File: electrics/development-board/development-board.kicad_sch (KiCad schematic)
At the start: 36 parts, among them J1 East, J10 Ext_5V, J8 West, J9 PinOut, Q3 S8050, Q4 S8050, SW1 Reset, SW2 Setup, SW3 Power, U1 LD1117S33

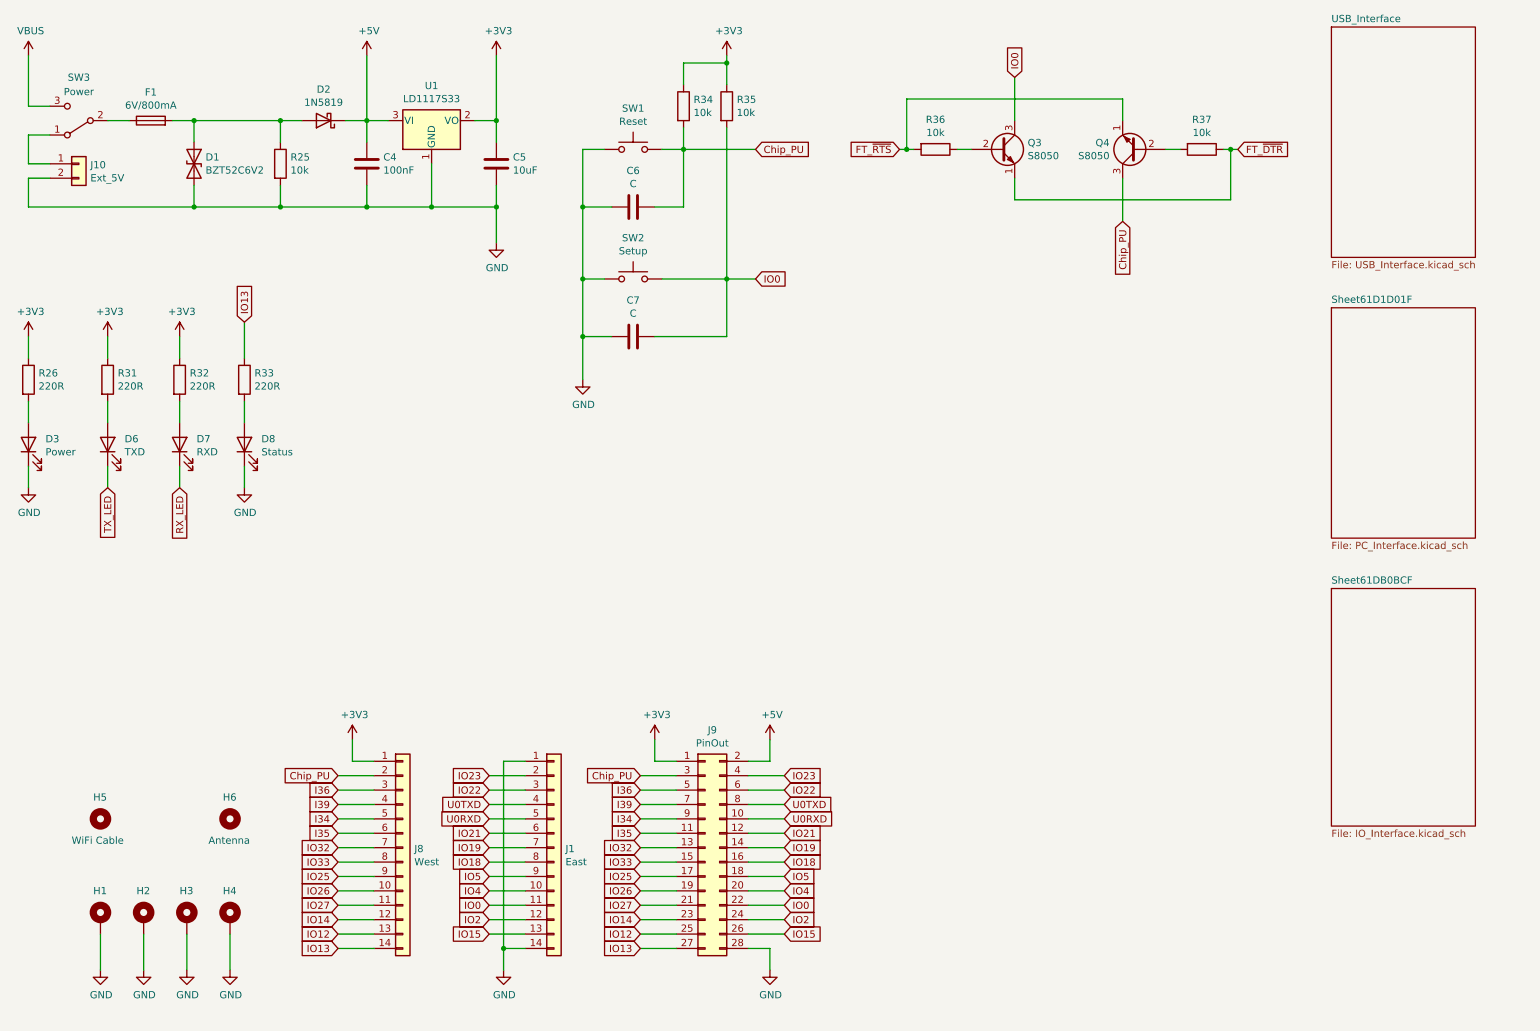
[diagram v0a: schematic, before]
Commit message: INOA-372 Rename Fab and Dev board
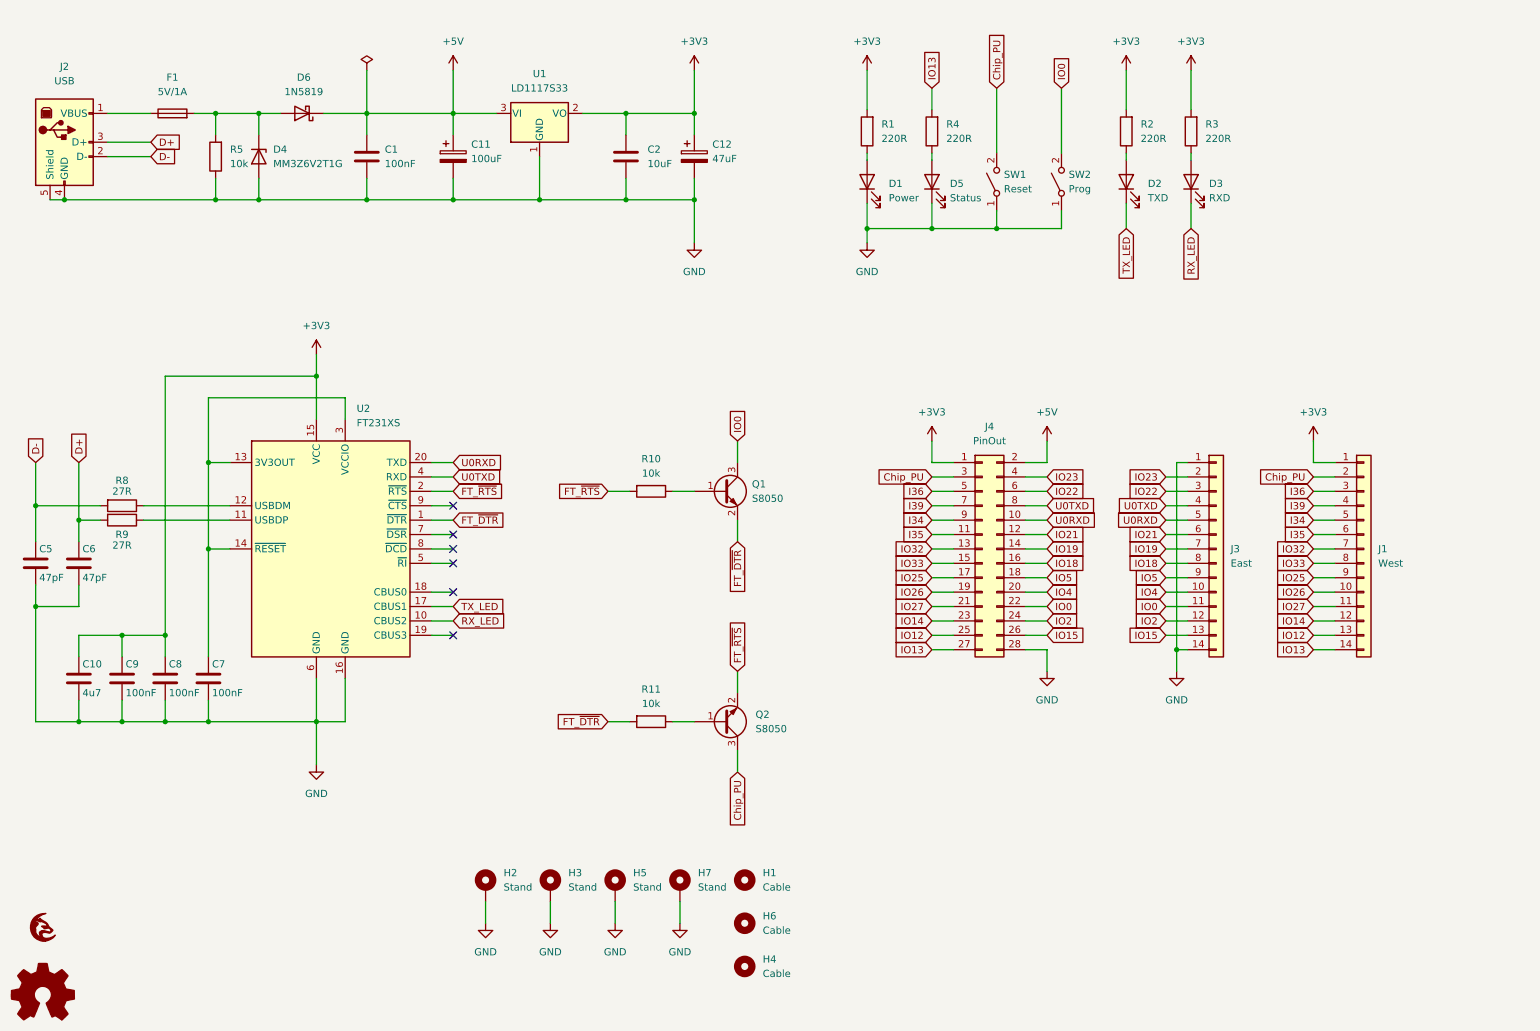
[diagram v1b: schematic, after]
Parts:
- removed C4: 100nF, Capacitor_SMD:C_1206_3216Metric_Pad1.33x1.80mm_HandSolder, symbol Device:C
- removed D1: BZT52C6V2, Diode_SMD:D_SOD-323_HandSoldering, symbol Device:D_TVS
- removed D2: 1N5819, Diode_SMD:D_SOD-323_HandSoldering, symbol Diode:1N5819
- removed D6: TXD, LED_SMD:LED_1206_3216Metric_Pad1.42x1.75mm_HandSolder, symbol Device:LED
- removed D7: RXD, LED_SMD:LED_1206_3216Metric_Pad1.42x1.75mm_HandSolder, symbol Device:LED
- removed D8: Status, LED_SMD:LED_1206_3216Metric_Pad1.42x1.75mm_HandSolder, symbol Device:LED
- removed H1, H4: MountingHole_Pad, MountingHole:MountingHole_3.2mm_M3_DIN965_Pad, symbol Mechanical:MountingHole_Pad
- removed H5: WiFi Cable, MountingHole:MountingHole_5.5mm, symbol Mechanical:MountingHole
- removed J10: Ext_5V, Connector_PinHeader_2.54mm:PinHeader_1x02_P2.54mm_Horizontal, symbol Connector_Generic:Conn_01x02
- removed J8: West, Connector_PinHeader_2.54mm:PinHeader_1x14_P2.54mm_Vertical, symbol Connector_Generic:Conn_01x14
- removed J9: PinOut, Connector_PinHeader_2.54mm:PinHeader_2x14_P2.54mm_Vertical, symbol Connector_Generic:Conn_02x14_Odd_Even
- removed Q3, Q4: S8050, Package_TO_SOT_SMD:SOT-23, symbol Transistor_BJT:S8050
- removed R25, R34, R35, R36, R37: 10k, Resistor_SMD:R_1206_3216Metric_Pad1.30x1.75mm_HandSolder, symbol Device:R
- removed R26, R31, R32, R33: 220R, Resistor_SMD:R_1206_3216Metric_Pad1.30x1.75mm_HandSolder, symbol Device:R
- removed SW1: Reset, Button_Switch_SMD:SW_SPST_PTS645, symbol Switch:SW_Push
- removed SW2: Setup, Button_Switch_SMD:SW_SPST_PTS645, symbol Switch:SW_Push
- removed SW3: Power, Button_Switch_THT:SW_E-Switch_EG1224_SPDT_Angled, symbol Switch:SW_SPDT
- added C1, C8, C9: 100nF, Capacitor_SMD:C_1206_3216Metric_Pad1.33x1.80mm_HandSolder, symbol Device:C
- added C10: 4u7, Capacitor_SMD:C_1206_3216Metric_Pad1.33x1.80mm_HandSolder, symbol Device:C
- added C11: 100uF, Capacitor_SMD:CP_Elec_6.3x5.4, symbol Device:C_Polarized
- added C12: 47uF, Capacitor_SMD:CP_Elec_6.3x5.4, symbol Device:C_Polarized
- added C2: 10uF, Capacitor_SMD:C_1206_3216Metric_Pad1.33x1.80mm_HandSolder, symbol Device:C
- added D1: Power, LED_SMD:LED_1206_3216Metric_Pad1.42x1.75mm_HandSolder, symbol Device:LED
- added D2: TXD, LED_SMD:LED_1206_3216Metric_Pad1.42x1.75mm_HandSolder, symbol Device:LED
- added D4: MM3Z6V2T1G, Diode_SMD:D_SOD-123F, symbol Diode:BZT52Bxx
- added D5: Status, LED_SMD:LED_1206_3216Metric_Pad1.42x1.75mm_HandSolder, symbol Device:LED
- added D6: 1N5819, Diode_SMD:D_SOD-323_HandSoldering, symbol Diode:1N5819
- added G1: LOGO, images:grayc-logo-negative, symbol grayc-logo-negative:LOGO
- added H1, H4: Cable, MountingHole:MountingHole_5.5mm, symbol Mechanical:MountingHole
- added H5, H7: Stand, MountingHole:MountingHole_3.2mm_M3_DIN965_Pad, symbol Mechanical:MountingHole_Pad
- added J2: USB, Connector_USB:USB_B_OST_USB-B1HSxx_Horizontal, symbol Connector:USB_B
- added J3: East, Connector_PinHeader_2.54mm:PinHeader_1x14_P2.54mm_Vertical, symbol Connector_Generic:Conn_01x14
- added J4: PinOut, Connector_PinHeader_2.54mm:PinHeader_2x14_P2.54mm_Vertical, symbol Connector_Generic:Conn_02x14_Odd_Even
- added LOGO1: Logo_Open_Hardware_Small, Symbol:OSHW-Logo2_7.3x6mm_SilkScreen, symbol Graphic:Logo_Open_Hardware_Small
- added Q1, Q2: S8050, Package_TO_SOT_SMD:SOT-23-3, symbol Device:Q_NPN_BEC
- added R1, R2, R3, R4: 220R, Resistor_SMD:R_1206_3216Metric_Pad1.30x1.75mm_HandSolder, symbol Device:R
- added R10, R11, R5: 10k, Resistor_SMD:R_1206_3216Metric_Pad1.30x1.75mm_HandSolder, symbol Device:R
- added R8, R9: 27R, Resistor_SMD:R_1206_3216Metric_Pad1.30x1.75mm_HandSolder, symbol Device:R
- added SW1: Reset, Button_Switch_SMD:SW_SPST_PTS645, symbol Switch:SW_SPST
- added SW2: Prog, Button_Switch_SMD:SW_SPST_PTS645, symbol Switch:SW_SPST
- added U2: FT231XS, Package_SO:SSOP-20_3.9x8.7mm_P0.635mm, symbol Interface_USB:FT231XS
- C5: value 10uF -> 47pF; #manf (none) -> C1206C470F3HACTU; #mouser (none) -> 80-C1206C470F3HACTU
- C6: value C -> 47pF; #manf (none) -> C1206C470F3HACTU; #mouser (none) -> 80-C1206C470F3HACTU
- C7: value C -> 100nF; #manf (none) -> C1206C104M5RACTU; #mouser (none) -> 80-C1206C104M5R
- D3: value Power -> RXD; #manf (none) -> SML-LXL1206GC-TR; #mouser (none) -> 696-SML-L1206GCTR
- F1: value 6V/800mA -> 5V/1A; #manf (none) -> TR/3216FF1-R; #mouser (none) -> 504-TR/3216FF1-R
- H2, H3: value MountingHole_Pad -> Stand
- H6: value Antenna -> Cable
- J1: value East -> West
- U1: #manf (none) -> LD1117S33CTR; #mouser (none) -> 511-LD1117S33C
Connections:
- net +3V3: now also J1.1 (Pin_1), C10.1, C12.1, C2.1, C8.1, C9.1, J4.1 (Pin_1), R1.2, R2.2, R3.2, U2.15 (VCC); no longer C5.1
- net +5V: now also C1.1, C11.1, D6.1 (K), J4.2 (Pin_2)
- net Chip_PU: now also J1.2 (Pin_2), J4.3 (Pin_3), Q2.3 (C), SW1.2 (B); no longer C6.1
- net FT_~{DTR}: now also Q1.2 (E), R11.2, U2.1 (~{DTR})
- net FT_~{RTS}: now also Q2.2 (E), R10.2, U2.2 (~{RTS})
- net GND: now also C1.2, C10.2, C11.2, C12.2, C2.2, C8.2, C9.2, D1.1 (K), D4.2 (A), D5.1 (K), H5.1, H7.1, J2.4 (GND), J2.5 (Shield), J3.1 (Pin_1), J3.14 (Pin_14), J4.28 (Pin_28), R5.1, SW1.1 (A), SW2.1 (A), U2.16 (GND), U2.6 (GND); no longer D3.1 (K), J1.1 (Pin_1), J1.14 (Pin_14)
- net I34: now also J1.5 (Pin_5), J4.9 (Pin_9)
- net I35: now also J1.6 (Pin_6), J4.11 (Pin_11)
- net I36: now also J1.3 (Pin_3), J4.5 (Pin_5)
- net I39: now also J1.4 (Pin_4), J4.7 (Pin_7)
- net IO0: now also J3.11 (Pin_11), J4.22 (Pin_22), Q1.3 (C), SW2.2 (B); no longer C7.1, J1.11 (Pin_11)
- net IO12: now also J1.13 (Pin_13), J4.25 (Pin_25)
- net IO13: now also J1.14 (Pin_14), J4.27 (Pin_27), R4.2
- net IO14: now also J1.12 (Pin_12), J4.23 (Pin_23)
- net IO15: now also J3.13 (Pin_13), J4.26 (Pin_26); no longer J1.13 (Pin_13)
- net IO18: now also J3.8 (Pin_8), J4.16 (Pin_16); no longer J1.8 (Pin_8)
- net IO19: now also J3.7 (Pin_7), J4.14 (Pin_14); no longer J1.7 (Pin_7)
- net IO2: now also J3.12 (Pin_12), J4.24 (Pin_24); no longer J1.12 (Pin_12)
- net IO21: now also J3.6 (Pin_6), J4.12 (Pin_12); no longer J1.6 (Pin_6)
- net IO22: now also J3.3 (Pin_3), J4.6 (Pin_6); no longer J1.3 (Pin_3)
- net IO23: now also J3.2 (Pin_2), J4.4 (Pin_4); no longer J1.2 (Pin_2)
- net IO25: now also J1.9 (Pin_9), J4.17 (Pin_17)
- net IO26: now also J1.10 (Pin_10), J4.19 (Pin_19)
- net IO27: now also J1.11 (Pin_11), J4.21 (Pin_21)
- net IO32: now also J1.7 (Pin_7), J4.13 (Pin_13)
- net IO33: now also J1.8 (Pin_8), J4.15 (Pin_15)
- net IO4: now also J3.10 (Pin_10), J4.20 (Pin_20); no longer J1.10 (Pin_10)
- net IO5: now also J3.9 (Pin_9), J4.18 (Pin_18); no longer J1.9 (Pin_9)
- net RX_LED: now also D3.1 (K), U2.10 (CBUS2)
- net TX_LED: now also D2.1 (K), U2.17 (CBUS1)
- net U0RXD: now also J3.5 (Pin_5), J4.10 (Pin_10), U2.20 (TXD); no longer J1.5 (Pin_5)
- net U0TXD: now also J3.4 (Pin_4), J4.8 (Pin_8), U2.4 (RXD); no longer J1.4 (Pin_4)
- net at D3.2 (A): now also R3.1
- net at F1.2: now also D4.1 (K), D6.2 (A), R5.2
- net at F1.1: now also J2.1 (VBUS)
- new net: Q2.1 (B), R11.1
- new net: C7.1, U2.13 (3V3OUT), U2.14 (~{RESET}), U2.3 (VCCIO)
- new net: R9.1, U2.11 (USBDP)
- new net: R8.1, U2.12 (USBDM)
- new net: D1.2 (A), R1.1
- new net: D5.2 (A), R4.1
- new net: D2.2 (A), R2.1
- new net: Q1.1 (B), R10.1
- new net D+: C6.1, J2.3 (D+), R9.2
- new net D-: C5.1, J2.2 (D-), R8.2
- no-connect marks 0 -> 6
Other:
- removed sheet Sheet61D1D01F
- removed sheet Sheet61DB0BCF
- removed sheet USB_Interface
